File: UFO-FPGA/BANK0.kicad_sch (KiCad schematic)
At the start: 7 parts, among them U1 ICE40HX8K-BG121

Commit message: Explainer
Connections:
- net CTSn: now also U1.B9 (IOT_174)
- net DCDn: now also U1.C8 (IOT_179)
- net DSRn: now also U1.A9 (IOT_178)
- net DTRn: now also U1.B8 (IOT_177)
- net RS232_Rx_TTL: now also U1.A11 (IOT_168)
- net RS232_Tx_TTL: now also U1.A10 (IOT_170)
- net RTSn: now also U1.C9 (IOT_172)
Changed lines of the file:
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@@
   (junction (at 151.13 35.56) (diameter 0) (color 0 0 0 0)
+  )
+  (wire (pts (xy 92.71 59.69) (xy 105.41 59.69))
+    (stroke (width 0) (type default))
   )
   (wire (pts (xy 151.13 35.56) (xy 162.56 35.56))
@@
     (stroke (width 0) (type default))
   )
+  (wire (pts (xy 92.71 62.23) (xy 105.41 62.23))
+    (stroke (width 0) (type default))
+  )
   (wire (pts (xy 151.13 35.56) (xy 139.7 35.56))
+    (stroke (width 0) (type default))
+  )
+  (wire (pts (xy 92.71 69.85) (xy 105.41 69.85))
     (stroke (width 0) (type default))
   )
@@
     (stroke (width 0) (type default))
   )
+  (wire (pts (xy 92.71 72.39) (xy 105.41 72.39))
+    (stroke (width 0) (type default))
+  )
   (wire (pts (xy 181.61 25.4) (xy 181.61 35.56))
     (stroke (width 0) (type default))
   )
+  (wire (pts (xy 92.71 74.93) (xy 105.41 74.93))
+    (stroke (width 0) (type default))
+  )
   (wire (pts (xy 151.13 43.18) (xy 162.56 43.18))
+    (stroke (width 0) (type default))
+  )
+  (wire (pts (xy 92.71 64.77) (xy 105.41 64.77))
     (stroke (width 0) (type default))
   )
@@
     (stroke (width 0) (type default))
   )
+  (wire (pts (xy 92.71 67.31) (xy 105.41 67.31))
+    (stroke (width 0) (type default))
+  )

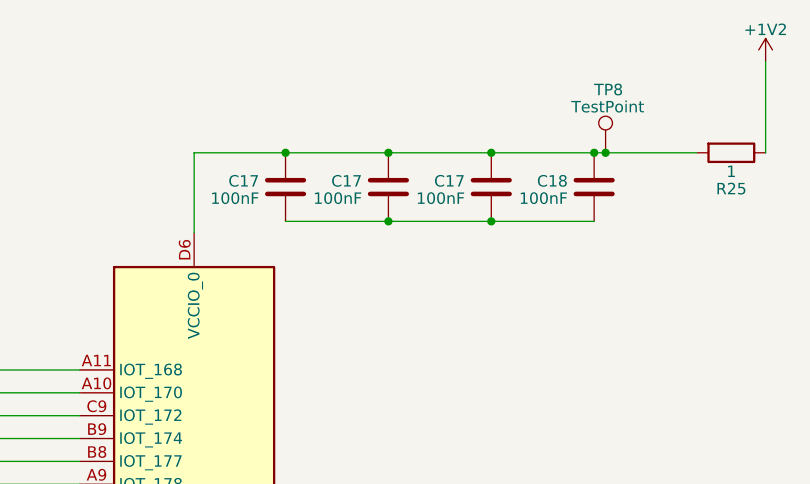
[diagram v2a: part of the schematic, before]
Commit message: Added net labels
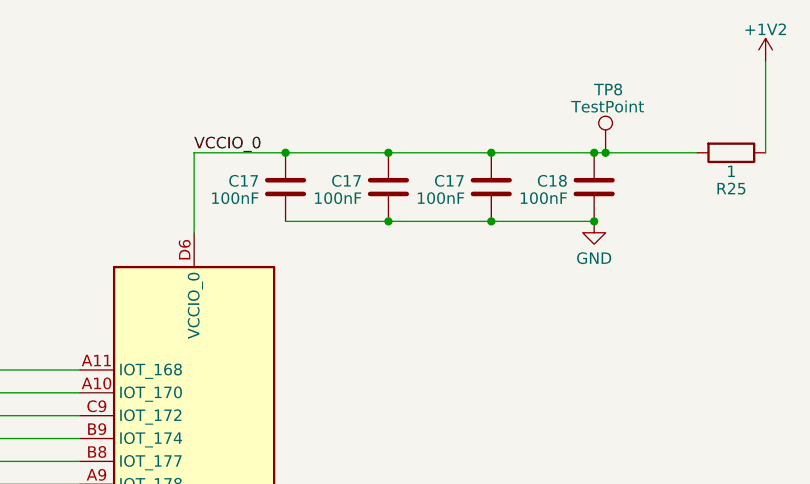
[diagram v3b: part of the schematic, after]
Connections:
- net VCCIO_0: now reaches C17.1, C17.1, C17.1, C18.1, R25.2, TP8.1, U1.D6 (VCCIO_0)
- net GND: now reaches C17.2, C17.2, C17.2, C18.2
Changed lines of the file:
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@@
   (junction (at 139.7 35.56) (diameter 0) (color 0 0 0 0)
   )
+  (junction (at 162.56 43.18) (diameter 0) (color 0 0 0 0)
+  )
   (junction (at 151.13 35.56) (diameter 0) (color 0 0 0 0)
   )
@@
   (wire (pts (xy 92.71 67.31) (xy 105.41 67.31))
     (stroke (width 0) (type default))
+  )
+  (label "VCCIO_0" (at 118.11 35.56 0) (fields_autoplaced)
+    (effects (font (size 1.27 1.27)) (justify left bottom))
   )
   (global_label "RS232_Rx_TTL" (shape input) (at 92.71 59.69 180) (fields_autoplaced)
@@
         )
       )
+    )
+  )
+  (symbol (lib_id "power:GND") (at 162.56 43.18 0) (unit 1)
+    (in_bom yes) (on_board yes) (dnp no) (fields_autoplaced)
+    (property "Reference" "#PWR037" (at 162.56 49.53 0)
+      (effects (font (size 1.27 1.27)) hide)
+    )
+    (property "Value" "GND" (at 162.56 47.3155 0)
+      (effects (font (size 1.27 1.27)))
+    )
+    (property "Footprint" "" (at 162.56 43.18 0)
+      (effects (font (size 1.27 1.27)) hide)
+    )
+    (property "Datasheet" "" (at 162.56 43.18 0)
+      (effects (font (size 1.27 1.27)) hide)
+    )
+    (pin "1")
+    (instances
+      (project "UFO-FPGA"
+        (path "/b3168f6a-c732-41d3-aeeb-d97dd2f1bb65/03eb349d-f783-448d-a9ad-735fd21dbf61"
+          (reference "#PWR037") (unit 1)
+        )
+      )

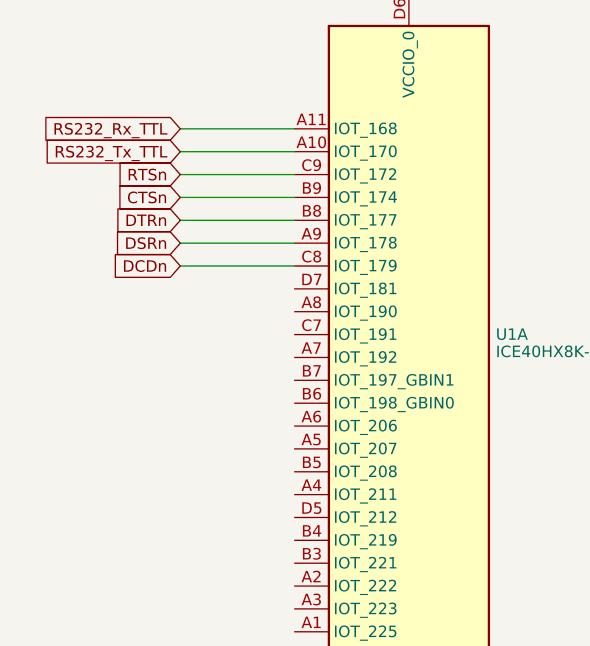
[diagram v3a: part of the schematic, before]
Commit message: Labels and schametic changes
Updated Power schematic
Added labes for the different nets
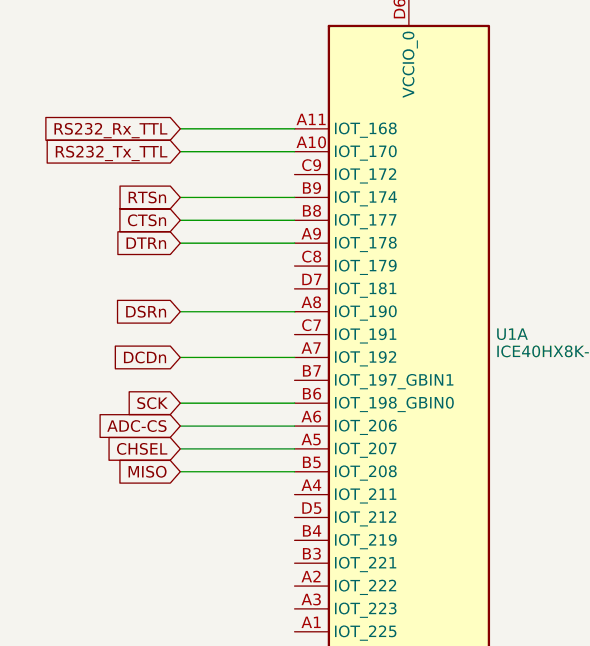
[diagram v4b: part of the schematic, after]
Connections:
- net CTSn: now also U1.B8 (IOT_177); no longer U1.B9 (IOT_174)
- net DCDn: now also U1.A7 (IOT_192); no longer U1.C8 (IOT_179)
- net DSRn: now also U1.A8 (IOT_190); no longer U1.A9 (IOT_178)
- net DTRn: now also U1.A9 (IOT_178); no longer U1.B8 (IOT_177)
- net RTSn: now also U1.B9 (IOT_174); no longer U1.C9 (IOT_172)
- net CHSEL: now reaches U1.A5 (IOT_207)
- net ADC-CS: now reaches U1.A6 (IOT_206)
- net MISO: now reaches U1.B5 (IOT_208)
- net SCK: now reaches U1.B6 (IOT_198_GBIN0)
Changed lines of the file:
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@@
+    (stroke (width 0) (type default))
+  )
+  (wire (pts (xy 92.71 97.79) (xy 105.41 97.79))
     (stroke (width 0) (type default))
   )
@@
     (stroke (width 0) (type default))
   )
+  (wire (pts (xy 92.71 95.25) (xy 105.41 95.25))
+    (stroke (width 0) (type default))
+  )
   (wire (pts (xy 151.13 35.56) (xy 139.7 35.56))
     (stroke (width 0) (type default))
   )
+  (wire (pts (xy 92.71 85.09) (xy 105.41 85.09))
+    (stroke (width 0) (type default))
+  )
+  (wire (pts (xy 92.71 72.39) (xy 105.41 72.39))
+    (stroke (width 0) (type default))
+  )
+  (wire (pts (xy 151.13 43.18) (xy 139.7 43.18))
+    (stroke (width 0) (type default))
+  )
+  (wire (pts (xy 128.27 35.56) (xy 118.11 35.56))
+    (stroke (width 0) (type default))
+  )
+  (wire (pts (xy 163.83 35.56) (xy 173.99 35.56))
+    (stroke (width 0) (type default))
+  )
+  (wire (pts (xy 139.7 35.56) (xy 128.27 35.56))
+    (stroke (width 0) (type default))
+  )
+  (wire (pts (xy 181.61 25.4) (xy 181.61 35.56))
+    (stroke (width 0) (type default))
+  )
+  (wire (pts (xy 92.71 67.31) (xy 105.41 67.31))
+    (stroke (width 0) (type default))
+  )
   (wire (pts (xy 92.71 69.85) (xy 105.41 69.85))
     (stroke (width 0) (type default))
   )
-  (wire (pts (xy 151.13 43.18) (xy 139.7 43.18))
-    (stroke (width 0) (type default))
-  )
-  (wire (pts (xy 128.27 35.56) (xy 118.11 35.56))
-    (stroke (width 0) (type default))
-  )
-  (wire (pts (xy 163.83 35.56) (xy 173.99 35.56))
-    (stroke (width 0) (type default))
-  )
-  (wire (pts (xy 139.7 35.56) (xy 128.27 35.56))
-    (stroke (width 0) (type default))
-  )
-  (wire (pts (xy 92.71 72.39) (xy 105.41 72.39))
-    (stroke (width 0) (type default))
-  )
-  (wire (pts (xy 181.61 25.4) (xy 181.61 35.56))
-    (stroke (width 0) (type default))
-  )
-  (wire (pts (xy 92.71 74.93) (xy 105.41 74.93))
-    (stroke (width 0) (type default))
-  )
   (wire (pts (xy 151.13 43.18) (xy 162.56 43.18))
     (stroke (width 0) (type default))
   )
-  (wire (pts (xy 92.71 64.77) (xy 105.41 64.77))
-    (stroke (width 0) (type default))
-  )
   (wire (pts (xy 118.11 35.56) (xy 118.11 44.45))
     (stroke (width 0) (type default))
   )
+  (wire (pts (xy 92.71 90.17) (xy 105.41 90.17))
+    (stroke (width 0) (type default))
+  )
+  (wire (pts (xy 92.71 80.01) (xy 105.41 80.01))
+    (stroke (width 0) (type default))
+  )
   (wire (pts (xy 139.7 43.18) (xy 128.27 43.18))
     (stroke (width 0) (type default))
   )
-  (wire (pts (xy 92.71 67.31) (xy 105.41 67.31))
+  (wire (pts (xy 92.71 92.71) (xy 105.41 92.71))
     (stroke (width 0) (type default))
   )
@@
     (effects (font (size 1.27 1.27)) (justify left bottom))
   )
+  (global_label "ADC-CS" (shape input) (at 92.71 92.71 180) (fields_autoplaced)
+    (effects (font (size 1.27 1.27)) (justify right))
+    (property "Intersheetrefs" "${INTERSHEET_REFS}" (at 82.1237 92.71 0)
+      (effects (font (size 1.27 1.27)) (justify right) hide)
+    )
+  )
   (global_label "RS232_Rx_TTL" (shape input) (at 92.71 59.69 180) (fields_autoplaced)
     (effects (font (size 1.27 1.27)) (justify right))
@@
     )
   )
-  (global_label "DCDn" (shape input) (at 92.71 74.93 180) (fields_autoplaced)
-    (effects (font (size 1.27 1.27)) (justify right))
-    (property "Intersheetrefs" "${INTERSHEET_REFS}" (at 84.8452 74.93 0)
+  (global_label "DCDn" (shape input) (at 92.71 85.09 180) (fields_autoplaced)
+    (effects (font (size 1.27 1.27)) (justify right))
+    (property "Intersheetrefs" "${INTERSHEET_REFS}" (at 84.8452 85.09 0)
       (effects (font (size 1.27 1.27)) (justify right) hide)
     )
@@
     )
   )
-  (global_label "RTSn" (shape input) (at 92.71 64.77 180) (fields_autoplaced)
-    (effects (font (size 1.27 1.27)) (justify right))
-    (property "Intersheetrefs" "${INTERSHEET_REFS}" (at 85.2081 64.77 0)
-      (effects (font (size 1.27 1.27)) (justify right) hide)
-    )
-  )
-  (global_label "CTSn" (shape input) (at 92.71 67.31 180) (fields_autoplaced)
+  (global_label "RTSn" (shape input) (at 92.71 67.31 180) (fields_autoplaced)
     (effects (font (size 1.27 1.27)) (justify right))
     (property "Intersheetrefs" "${INTERSHEET_REFS}" (at 85.2081 67.31 0)
@@
     )
   )
-  (global_label "DTRn" (shape input) (at 92.71 69.85 180) (fields_autoplaced)
-    (effects (font (size 1.27 1.27)) (justify right))
-    (property "Intersheetrefs" "${INTERSHEET_REFS}" (at 85.1476 69.85 0)
-      (effects (font (size 1.27 1.27)) (justify right) hide)
-    )
-  )
-  (global_label "DSRn" (shape input) (at 92.71 72.39 180) (fields_autoplaced)
-    (effects (font (size 1.27 1.27)) (justify right))
-    (property "Intersheetrefs" "${INTERSHEET_REFS}" (at 84.9057 72.39 0)
+  (global_label "SCK" (shape input) (at 92.71 90.17 180) (fields_autoplaced)
+    (effects (font (size 1.27 1.27)) (justify right))
+    (property "Intersheetrefs" "${INTERSHEET_REFS}" (at 86.0547 90.17 0)
+      (effects (font (size 1.27 1.27)) (justify right) hide)
+    )
+  )
+  (global_label "CTSn" (shape input) (at 92.71 69.85 180) (fields_autoplaced)
+    (effects (font (size 1.27 1.27)) (justify right))
+    (property "Intersheetrefs" "${INTERSHEET_REFS}" (at 85.2081 69.85 0)
+      (effects (font (size 1.27 1.27)) (justify right) hide)
+    )
+  )
+  (global_label "CHSEL" (shape input) (at 92.71 95.25 180) (fields_autoplaced)
+    (effects (font (size 1.27 1.27)) (justify right))
+    (property "Intersheetrefs" "${INTERSHEET_REFS}" (at 83.8171 95.25 0)
+      (effects (font (size 1.27 1.27)) (justify right) hide)
+    )
+  )
+  (global_label "MISO" (shape input) (at 92.71 97.79 180) (fields_autoplaced)
+    (effects (font (size 1.27 1.27)) (justify right))
+    (property "Intersheetrefs" "${INTERSHEET_REFS}" (at 85.208 97.79 0)
+      (effects (font (size 1.27 1.27)) (justify right) hide)
+    )
+  )
+  (global_label "DTRn" (shape input) (at 92.71 72.39 180) (fields_autoplaced)
+    (effects (font (size 1.27 1.27)) (justify right))
+    (property "Intersheetrefs" "${INTERSHEET_REFS}" (at 85.1476 72.39 0)
+      (effects (font (size 1.27 1.27)) (justify right) hide)
+    )
+  )
+  (global_label "DSRn" (shape input) (at 92.71 80.01 180) (fields_autoplaced)
+    (effects (font (size 1.27 1.27)) (justify right))
+    (property "Intersheetrefs" "${INTERSHEET_REFS}" (at 84.9057 80.01 0)
       (effects (font (size 1.27 1.27)) (justify right) hide)
     )
@@
   (symbol (lib_id "power:GND") (at 162.56 43.18 0) (unit 1)
     (in_bom yes) (on_board yes) (dnp no) (fields_autoplaced)
-    (property "Reference" "#PWR037" (at 162.56 49.53 0)
+    (property "Reference" "#PWR0101" (at 162.56 49.53 0)
       (effects (font (size 1.27 1.27)) hide)
     )
@@
       (project "UFO-FPGA"
         (path "/b3168f6a-c732-41d3-aeeb-d97dd2f1bb65/03eb349d-f783-448d-a9ad-735fd21dbf61"
-          (reference "#PWR037") (unit 1)
-        )
-      )
+          (reference "#PWR0101") (unit 1)
+        )
+      )
